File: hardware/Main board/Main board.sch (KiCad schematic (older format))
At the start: 78 parts, among them J1 Wind Direction, J2 Wind Speed, J3 USB_B_Micro, J4 Micro_SD_Card, J5 Sensor board connector, J6 Barrel_Jack, J7 USB programmer, SW1 SW_Push, SW2 SW_SPST, U1 FT232RL, U2 MCP6042, U3 SCWN03A-03, U4 ATmega1284P-AU, U5 DS3231M, U6 ENC28J60, U7 USB6B1, Y1 16MHZ

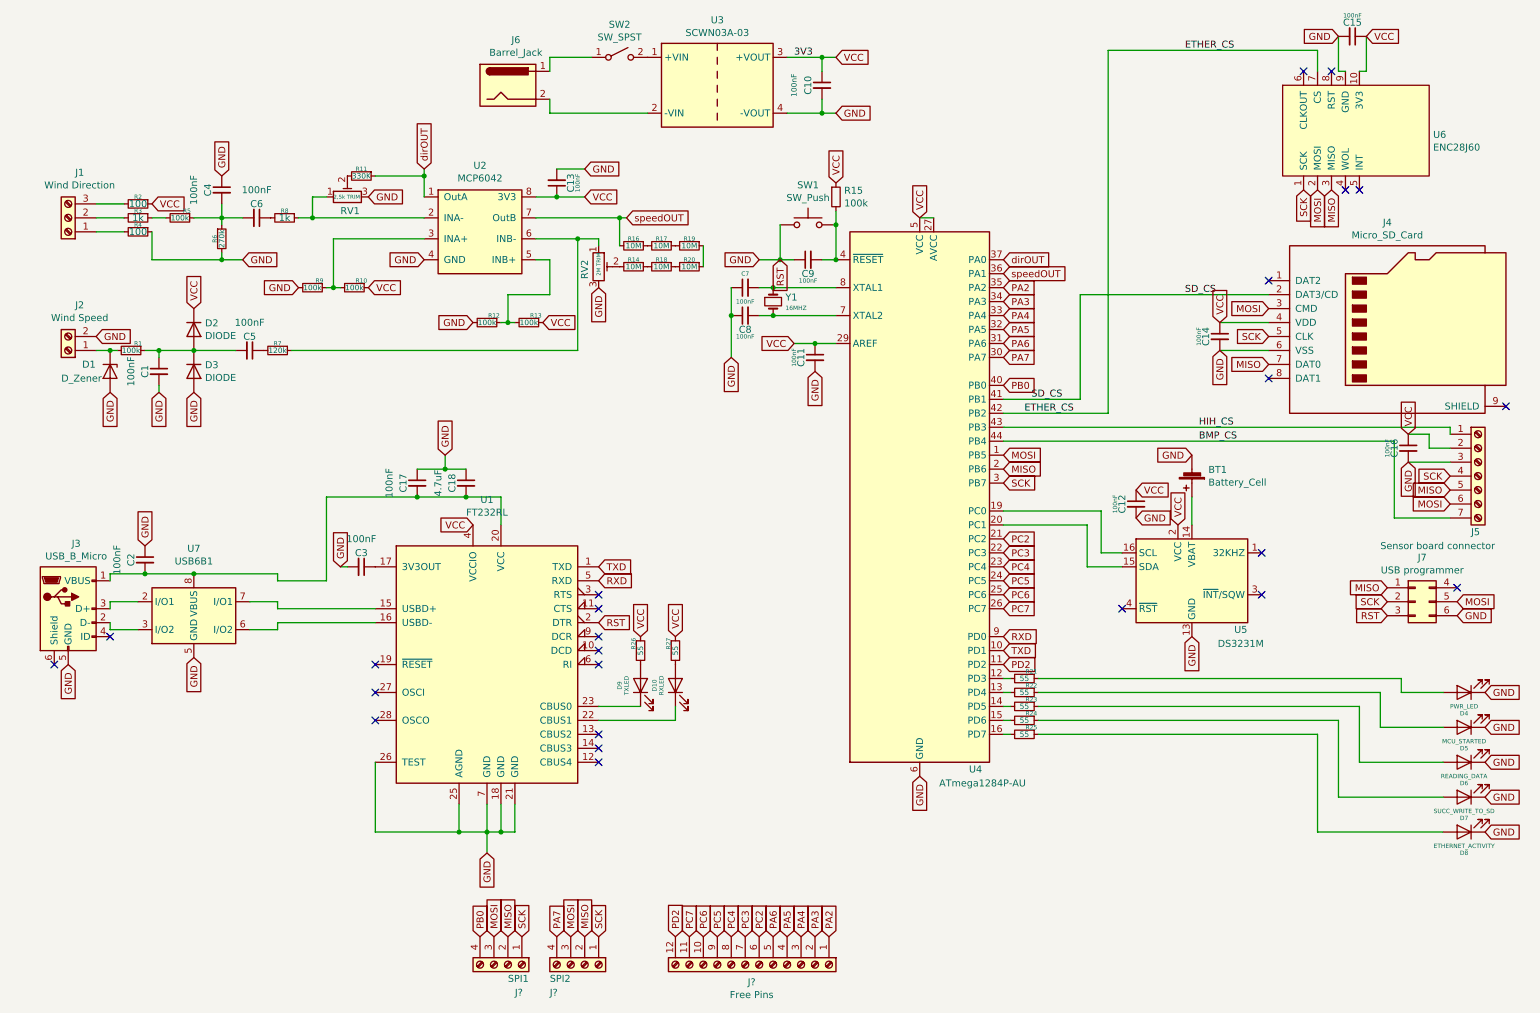
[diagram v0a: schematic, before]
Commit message: Added main board.
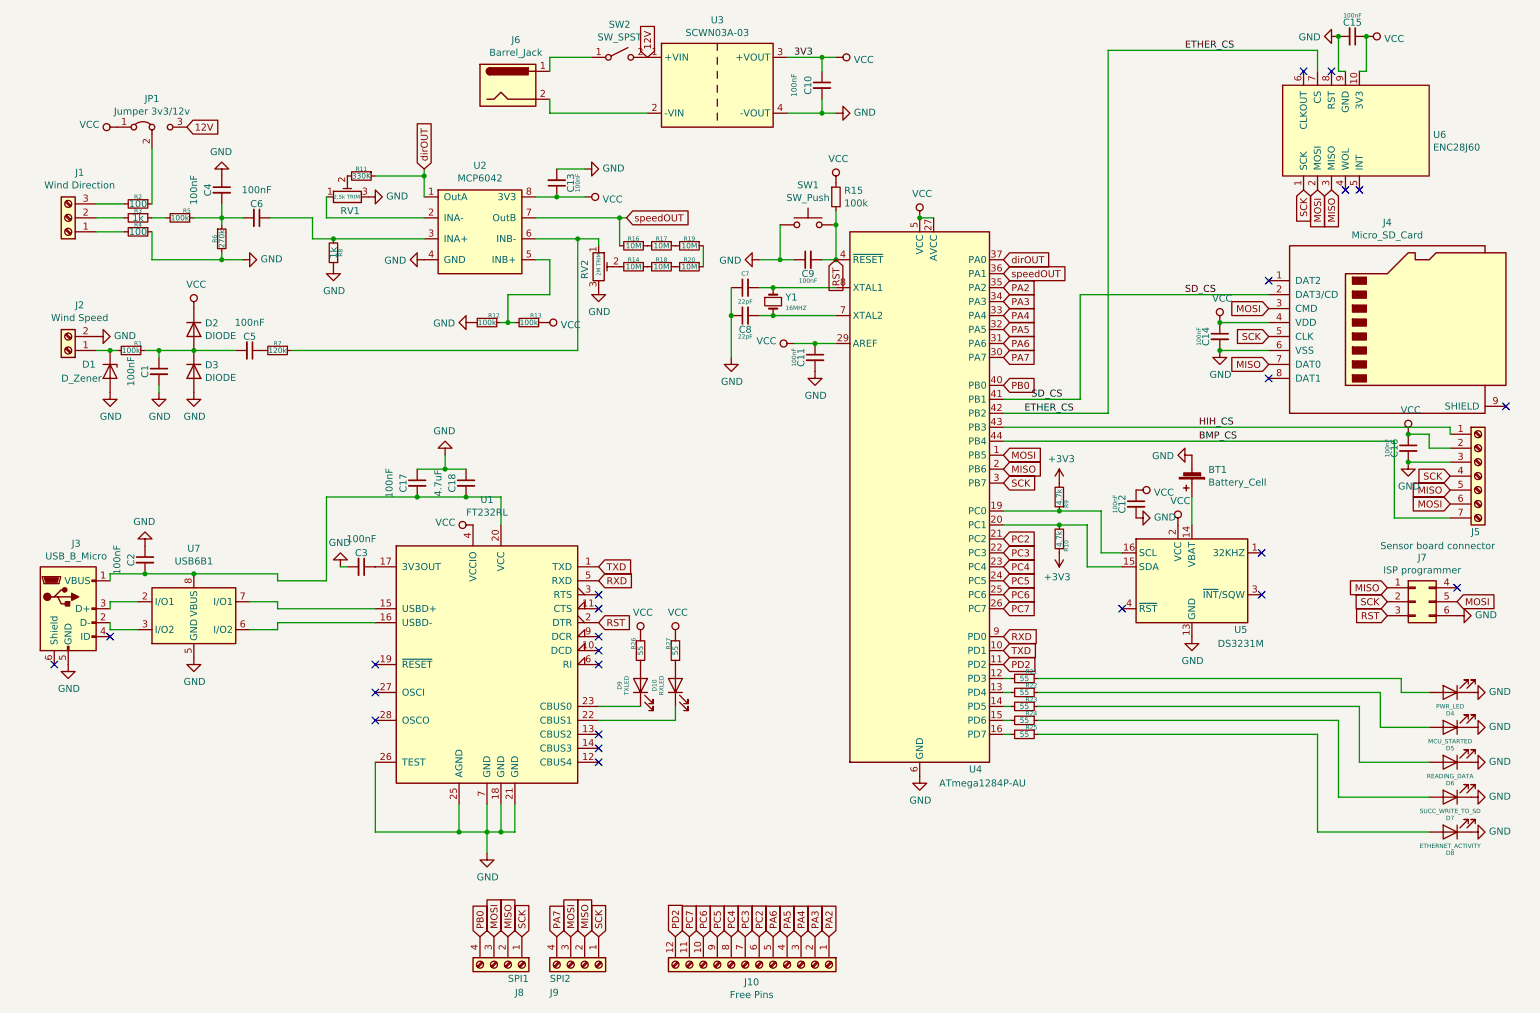
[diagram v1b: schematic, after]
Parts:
- added JP1: Jumper 3v3/12v, symbol Jumper:Jumper_3_Bridged12
- C7, C8: value 100nF -> 22pF
- J1: footprint TerminalBlock:TerminalBlock_Altech_AK300-3_P5.00mm -> TerminalBlock:TerminalBlock_Altech_AK300-4_P5.00mm
- J10: renamed from J?; footprint (none) -> TerminalBlock_Phoenix:TerminalBlock_Phoenix_MKDS-1,5-14_1x14_P5.00mm_Horizontal
- J5: footprint TerminalBlock_4Ucon:TerminalBlock_4Ucon_1x07_P3.50mm_Vertical -> TerminalBlock_Phoenix:TerminalBlock_Phoenix_MKDS-1,5-7_1x07_P5.00mm_Horizontal
- J7: value USB programmer -> ISP programmer
- J8, J9: renamed from J?; footprint (none) -> TerminalBlock:TerminalBlock_Altech_AK300-4_P5.00mm
- R10, R9: value 100k -> 4.7k
- U2: footprint (none) -> Meteo footprints:MCP6042-E&slash_P
- U3: footprint Converter_DCDC:Converter_DCDC_Artesyn_ATA_SMD -> Meteo footprints:SCWN03A
- U6: footprint (none) -> Meteo footprints:ENC28J60
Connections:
- net GND: now also R8.1; no longer J7.3 (Pin_3), R9.2, U1.2 (DTR)
- net VCC: now also JP1.1 (A); no longer R10.1, R2.1
- net at U4.19 (PC0), U5.16 (SCL): now also R9.1
- net at U4.20 (PC1), U5.15 (SDA): now also R10.2
- net RST: now reaches C9.2, R15.2, SW1.2, U4.4 (~RESET)
- net RST: now also J7.3 (Pin_3), U1.2 (DTR)
- net at RV1.1, U2.2 (INA-): no longer R8.1
- net at C6.1, R8.2: now also U2.3 (INA+)
- net 12V: now reaches SW2.2 (B), U3.1 (+VIN)
- net 12V: now also JP1.3 (B)
- new net: JP1.2 (C), R2.1
- new net +3V3: R10.1, R9.2
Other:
- moved on the sheet: D4, D5, D6, D7, D8

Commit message: Added a main board schematic
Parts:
- added C19, C20: 100nF, Capacitor_SMD:C_0805_2012Metric_Pad1.15x1.40mm_HandSolder, symbol Device:C_Small
- added R28, R29: 100k, Resistor_SMD:R_0805_2012Metric, symbol Device:R_Small
- added SW3, SW4: SW_Push, Button_Switch_SMD:Nidec_Copal_SH-7010A, symbol Switch:SW_Push
- J10: symbol Connector:Screw_Terminal_01x12 -> Connector:Screw_Terminal_01x10
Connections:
- net GND: now also C19.2, C20.2, SW3.2, SW4.2
- net PC6: now also C19.1, R28.2, SW3.1; no longer J10.10 (Pin_10)
- net PC7: now also C20.1, R29.2, SW4.1; no longer J10.11 (Pin_11)
- net PD2: now also J10.10 (Pin_10); no longer J10.12 (Pin_12)
- net VCC: now also R28.1, R29.1
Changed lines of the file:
@@
 	3550 3750 3700 3750
 $Comp
-L Connector:Screw_Terminal_01x12 J10
+L Connector:Screw_Terminal_01x10 J10
 U 1 1 5D5E4FDD
 P 5800 7300
@@
 Text GLabel 7550 4550 2    50   Input ~ 0
 PC5
-Text GLabel 7550 4650 2    50   Input ~ 0
-PC6
-Text GLabel 7550 4750 2    50   Input ~ 0
-PC7
 Text GLabel 7550 5150 2    50   Input ~ 0
 PD2
-Text GLabel 6300 7100 1    50   Input ~ 0
+Text GLabel 6200 7100 1    50   Input ~ 0
 PA2
-Text GLabel 6200 7100 1    50   Input ~ 0
+Text GLabel 6100 7100 1    50   Input ~ 0
 PA3
-Text GLabel 6100 7100 1    50   Input ~ 0
+Text GLabel 6000 7100 1    50   Input ~ 0
 PA4
-Text GLabel 6000 7100 1    50   Input ~ 0
+Text GLabel 5900 7100 1    50   Input ~ 0
 PA5
-Text GLabel 5900 7100 1    50   Input ~ 0
+Text GLabel 5800 7100 1    50   Input ~ 0
 PA6
 Text GLabel 4350 7100 1    50   Input ~ 0
@@
 Text GLabel 3800 7100 1    50   Input ~ 0
 PB0
-Text GLabel 5800 7100 1    50   Input ~ 0
+Text GLabel 5700 7100 1    50   Input ~ 0
 PC2
-Text GLabel 5700 7100 1    50   Input ~ 0
+Text GLabel 5600 7100 1    50   Input ~ 0
 PC3
-Text GLabel 5600 7100 1    50   Input ~ 0
+Text GLabel 5500 7100 1    50   Input ~ 0
 PC4
-Text GLabel 5500 7100 1    50   Input ~ 0
+Text GLabel 5400 7100 1    50   Input ~ 0
 PC5
-Text GLabel 5400 7100 1    50   Input ~ 0
-PC6
 Text GLabel 5300 7100 1    50   Input ~ 0
-PC7
-Text GLabel 5200 7100 1    50   Input ~ 0
 PD2
 $Comp
@@
 	1    0    0    -1
 $EndComp
+$Comp
+L Switch:SW_Push SW3
+U 1 1 5D3CBD40
+P 8150 6100
+F 0 "SW3" H 8150 6385 50  0000 C CNN
+F 1 "SW_Push" H 8150 6294 50  0000 C CNN
+F 2 "Button_Switch_SMD:Nidec_Copal_SH-7010A" H 8150 6300 50  0001 C CNN
+F 3 "~" H 8150 6300 50  0001 C CNN
+	1    8150 6100
+	1    0    0    -1
+$EndComp
+Text GLabel 7550 4650 2    50   Input ~ 0
+PC6
+Text GLabel 7550 4750 2    50   Input ~ 0
+PC7
+Text GLabel 7900 6300 0    50   Input ~ 0
+PC6
+$Comp
+L Device:C_Small C19
+U 1 1 5D3CFD9C
+P 8150 6300
+F 0 "C19" V 8050 6300 50  0000 C CNN
+F 1 "100nF" V 8000 6300 31  0000 C CNN
+F 2 "Capacitor_SMD:C_0805_2012Metric_Pad1.15x1.40mm_HandSolder" H 8150 6300 50  0001 C CNN
+F 3 "~" H 8150 6300 50  0001 C CNN
+	1    8150 6300
+	0    -1   -1   0
+$EndComp
+$Comp
+L Device:R_Small R28
+U 1 1 5D3D182E
+P 7950 6000
+F 0 "R28" H 8009 6046 50  0000 L CNN
+F 1 "100k" H 8009 5955 50  0000 L CNN
+F 2 "Resistor_SMD:R_0805_2012Metric" H 7950 6000 50  0001 C CNN
+F 3 "~" H 7950 6000 50  0001 C CNN
+	1    7950 6000
+	1    0    0    -1
+$EndComp
+$Comp
+L power:GND #PWR055
+U 1 1 5D3D2E07
+P 8350 6300
+F 0 "#PWR055" H 8350 6050 50  0001 C CNN
+F 1 "GND" V 8355 6172 50  0000 R CNN
+F 2 "" H 8350 6300 50  0001 C CNN
+F 3 "" H 8350 6300 50  0001 C CNN
+	1    8350 6300
+	0    -1   -1   0
+$EndComp
+Wire Wire Line
+	7950 6100 7950 6300
+Wire Wire Line
+	7950 6300 7900 6300
+Connection ~ 7950 6100
+Wire Wire Line
+	7950 6300 8050 6300
+Connection ~ 7950 6300
+Wire Wire Line
+	8350 6100 8350 6300
+Wire Wire Line
+	8350 6300 8250 6300
+Connection ~ 8350 6300
+$Comp
+L power:VCC #PWR054
+U 1 1 5D4070DD
+P 7950 5900
+F 0 "#PWR054" H 7950 5750 50  0001 C CNN
+F 1 "VCC" H 7967 6073 50  0000 C CNN
+F 2 "" H 7950 5900 50  0001 C CNN
+F 3 "" H 7950 5900 50  0001 C CNN
+	1    7950 5900
+	1    0    0    -1
+$EndComp
+$Comp
+L Device:R_Small R29
+U 1 1 5D4079F8
+P 8900 6000
+F 0 "R29" H 8959 6046 50  0000 L CNN
+F 1 "100k" H 8959 5955 50  0000 L CNN
+F 2 "Resistor_SMD:R_0805_2012Metric" H 8900 6000 50  0001 C CNN
+F 3 "~" H 8900 6000 50  0001 C CNN
+	1    8900 6000
+	1    0    0    -1
+$EndComp
+$Comp
+L Switch:SW_Push SW4
+U 1 1 5D40868C
+P 9100 6100
+F 0 "SW4" H 9100 6385 50  0000 C CNN
+F 1 "SW_Push" H 9100 6294 50  0000 C CNN
+F 2 "Button_Switch_SMD:Nidec_Copal_SH-7010A" H 9100 6300 50  0001 C CNN
+F 3 "~" H 9100 6300 50  0001 C CNN
+	1    9100 6100
+	1    0    0    -1
+$EndComp
+$Comp
+L Device:C_Small C20
+U 1 1 5D4090B1
+P 9100 6300
+F 0 "C20" V 9000 6300 50  0000 C CNN
+F 1 "100nF" V 8950 6300 31  0000 C CNN
+F 2 "Capacitor_SMD:C_0805_2012Metric_Pad1.15x1.40mm_HandSolder" H 9100 6300 50  0001 C CNN
+F 3 "~" H 9100 6300 50  0001 C CNN
+	1    9100 6300
+	0    -1   -1   0
+$EndComp
+$Comp
+L power:GND #PWR057
+U 1 1 5D409B4C
+P 9300 6300
+F 0 "#PWR057" H 9300 6050 50  0001 C CNN
+F 1 "GND" V 9305 6172 50  0000 R CNN
+F 2 "" H 9300 6300 50  0001 C CNN
+F 3 "" H 9300 6300 50  0001 C CNN
+	1    9300 6300
+	0    -1   -1   0
+$EndComp
+Wire Wire Line
+	8900 6100 8900 6300
+Wire Wire Line
+	8900 6300 9000 6300
+Connection ~ 8900 6100
+Wire Wire Line
+	9200 6300 9300 6300
+Wire Wire Line
+	9300 6100 9300 6300
+Connection ~ 9300 6300
+$Comp
+L power:VCC #PWR056
+U 1 1 5D4242BB
+P 8900 5900
+F 0 "#PWR056" H 8900 5750 50  0001 C CNN
+F 1 "VCC" H 8917 6073 50  0000 C CNN
+F 2 "" H 8900 5900 50  0001 C CNN
+F 3 "" H 8900 5900 50  0001 C CNN
+	1    8900 5900
+	1    0    0    -1
+$EndComp
+Text GLabel 8900 6300 0    50   Input ~ 0
+PC7
 $EndSCHEMATC

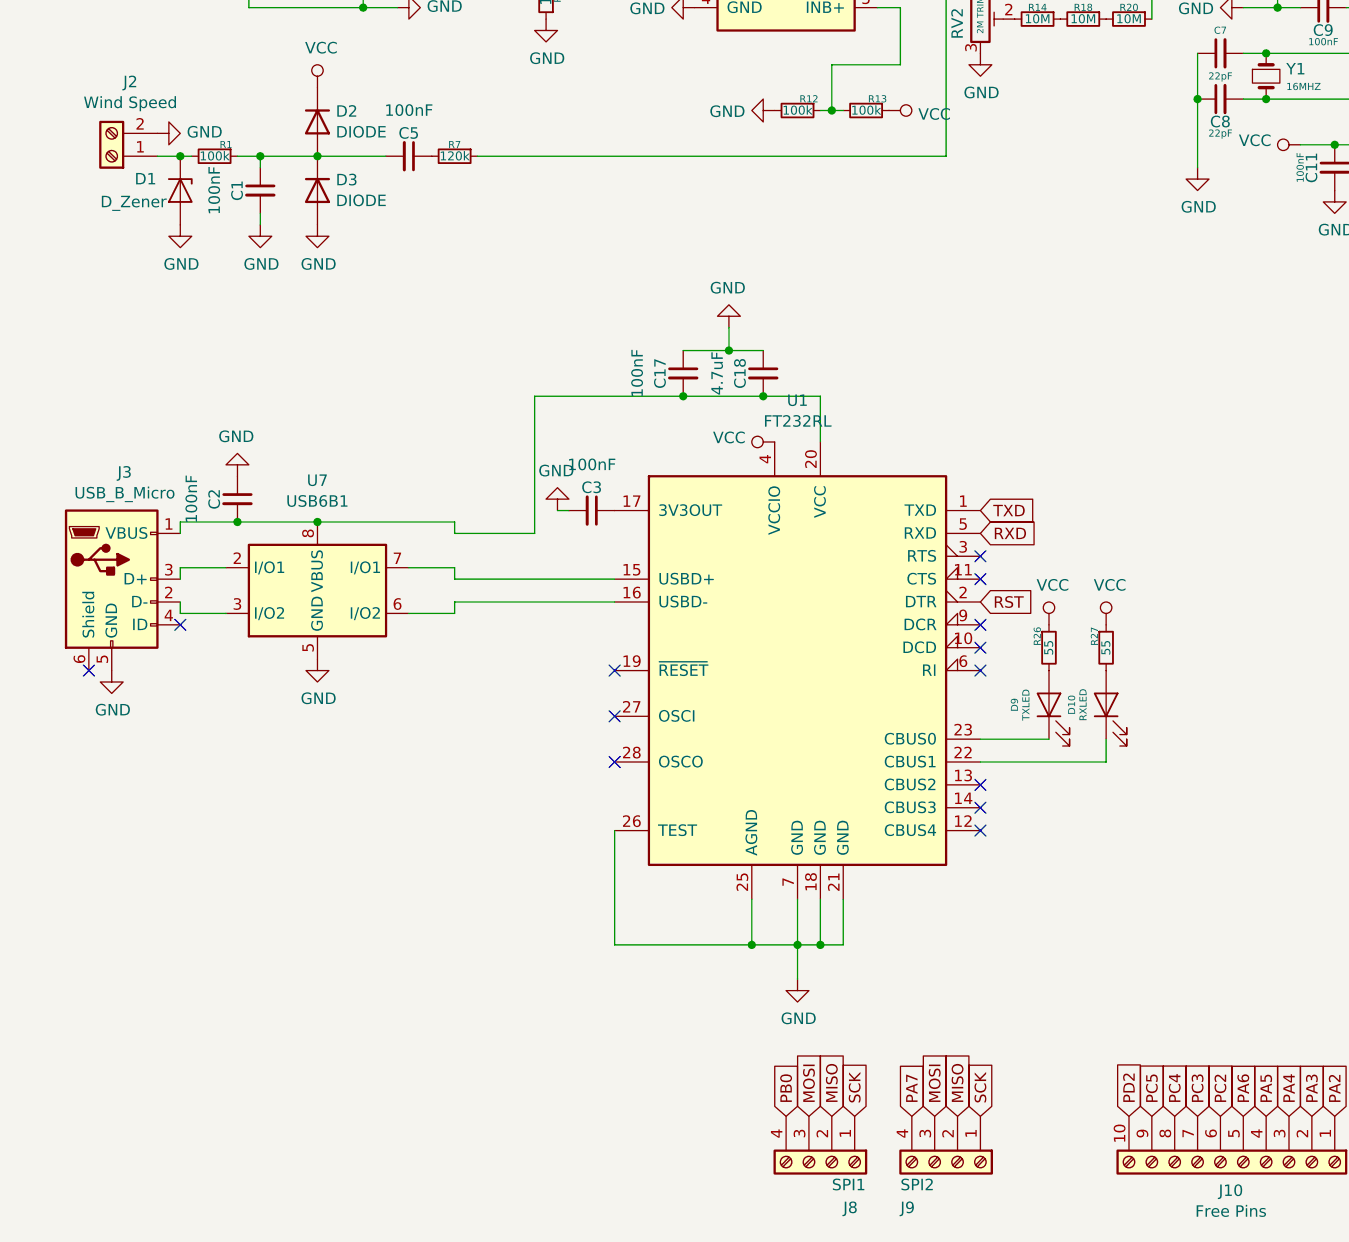
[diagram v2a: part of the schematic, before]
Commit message: Updated the board with nokia 5110 display.
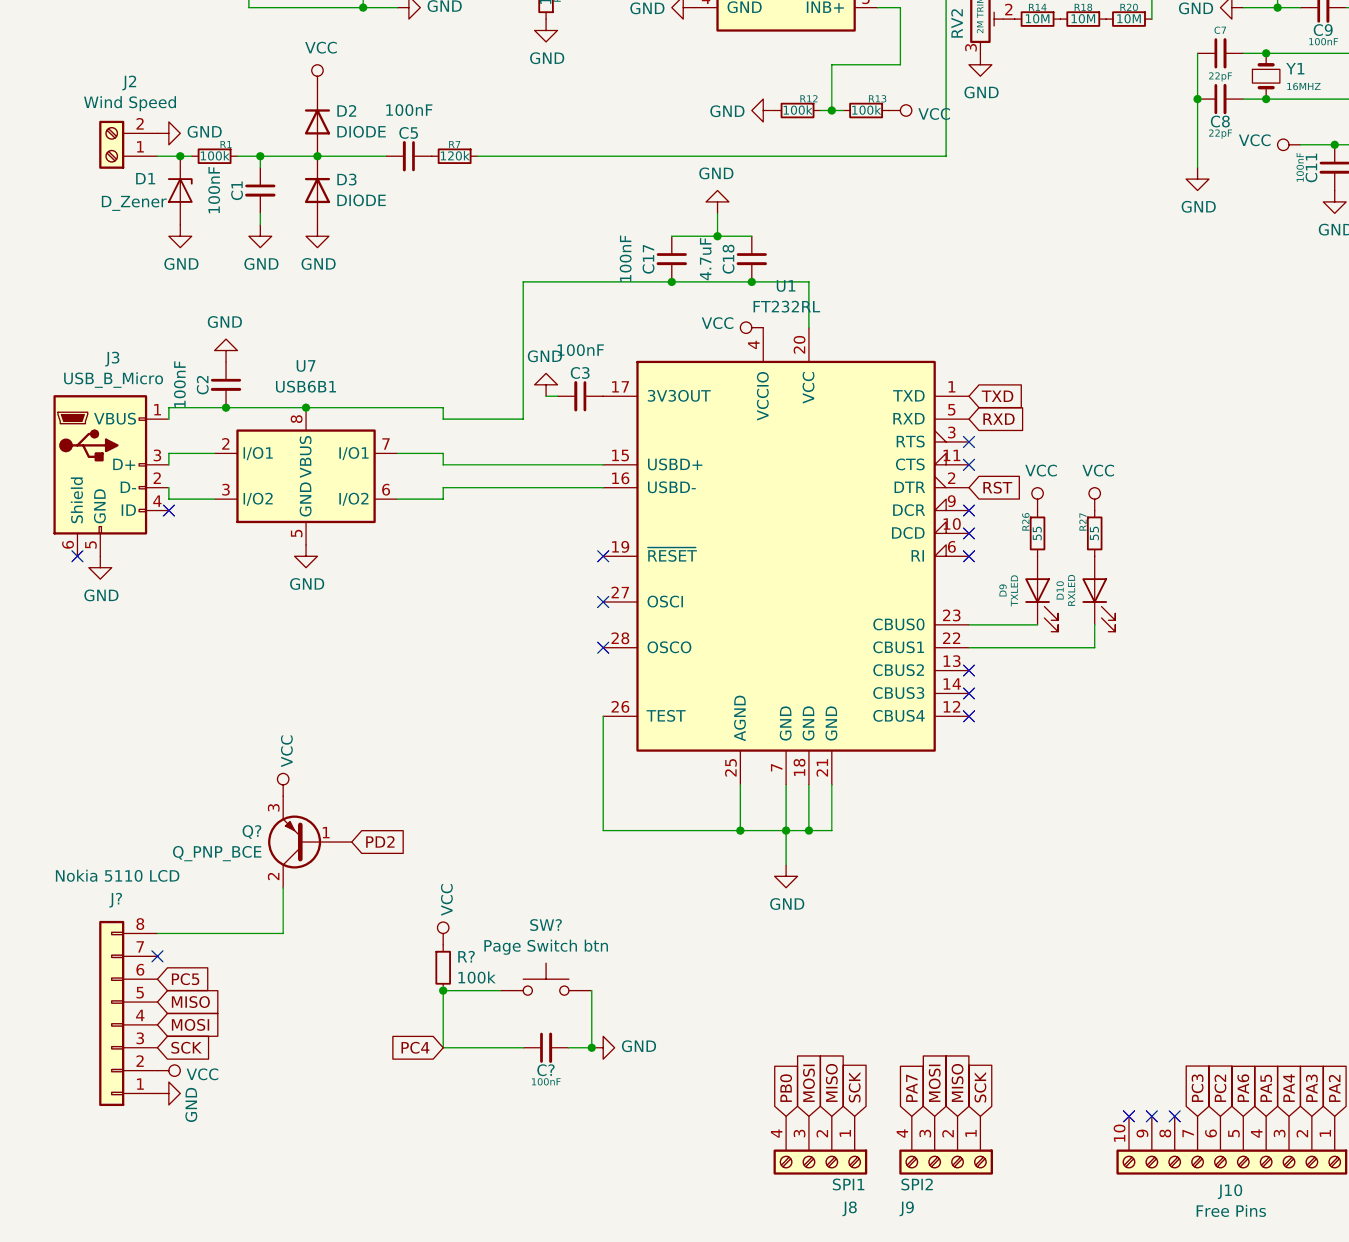
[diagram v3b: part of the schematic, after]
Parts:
- added C?: 100nF, Capacitor_SMD:C_0805_2012Metric_Pad1.15x1.40mm_HandSolder, symbol Device:C_Small
- added J?: Nokia 5110 LCD, symbol Connector_Generic:Conn_01x08
- added Q?: Q_PNP_BCE, symbol Device:Q_PNP_BCE
- added R?: 100k, Resistor_SMD:R_0805_2012Metric, symbol Device:R_Small
- added SW?: Page Switch btn, Button_Switch_SMD:Nidec_Copal_SH-7010A, symbol Switch:SW_Push
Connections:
- net GND: now also C?.2, J?.1 (Pin_1), SW?.2
- net MISO: now also J?.5 (Pin_5)
- net MOSI: now also J?.4 (Pin_4)
- net PC4: now also C?.1, R?.2, SW?.1; no longer J10.8 (Pin_8)
- net PC5: now also J?.6 (Pin_6); no longer J10.9 (Pin_9)
- net PD2: now also Q?.1 (B); no longer J10.10 (Pin_10)
- net SCK: now also J?.3 (Pin_3)
- net VCC: now also J?.2 (Pin_2), Q?.3 (E), R?.1
- new net: J?.8 (Pin_8), Q?.2 (C)
- no-connect marks 24 -> 28
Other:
- moved on the sheet: C17, C18, C2, C3, D10, D9, J3, R26, R27, U1, U7
